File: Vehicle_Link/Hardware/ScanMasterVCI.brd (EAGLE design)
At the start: 53 x 39.4 mm, 96 parts, among them IC1 XMEGA32A4U, IC2 TL331, IC3 TL331, IC4 TL331, IC5 TL331, Q1 MMBT4403, Q10 ZXMP6A17G, Q2 MMBT3904, Q3 RUM002N05, Q5 RUM002N05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

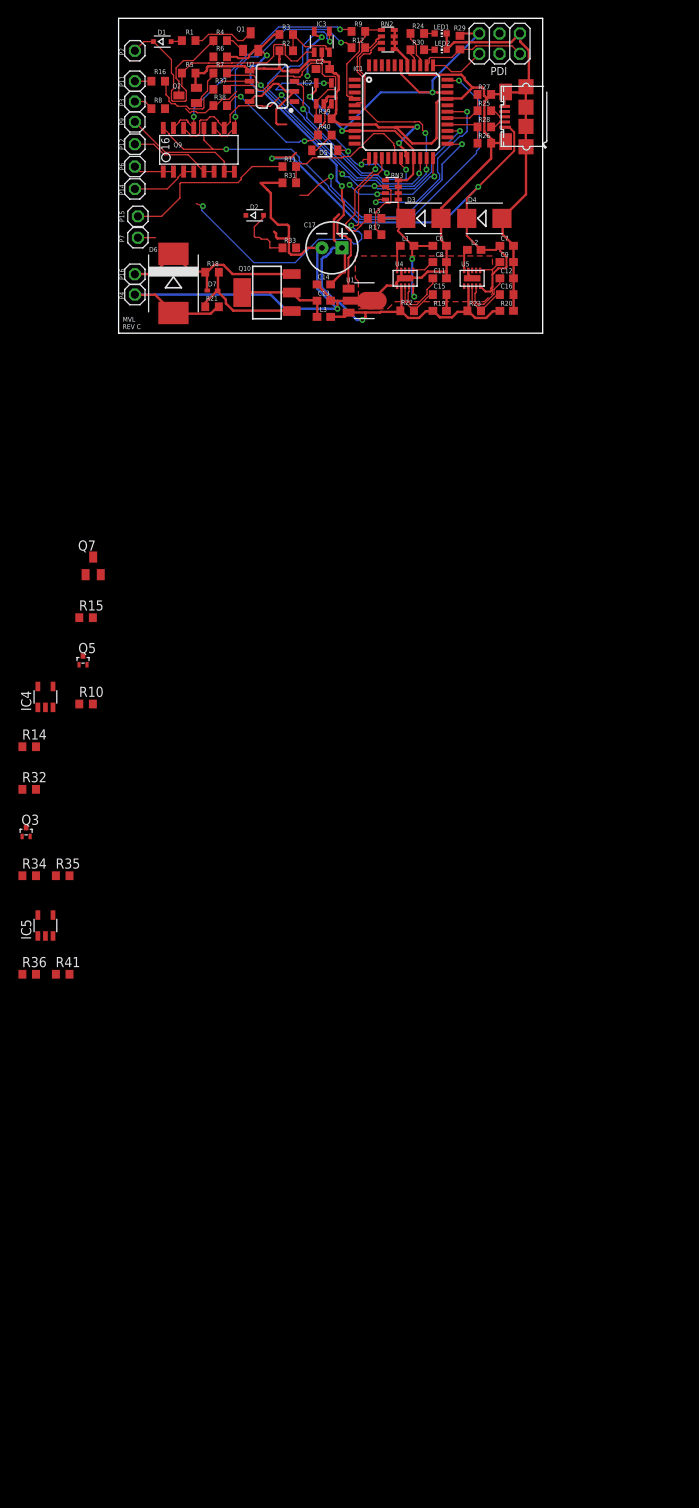
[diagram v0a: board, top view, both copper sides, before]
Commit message: Removed the BJTs I was using. Going to try the schematic with MOSFETs.
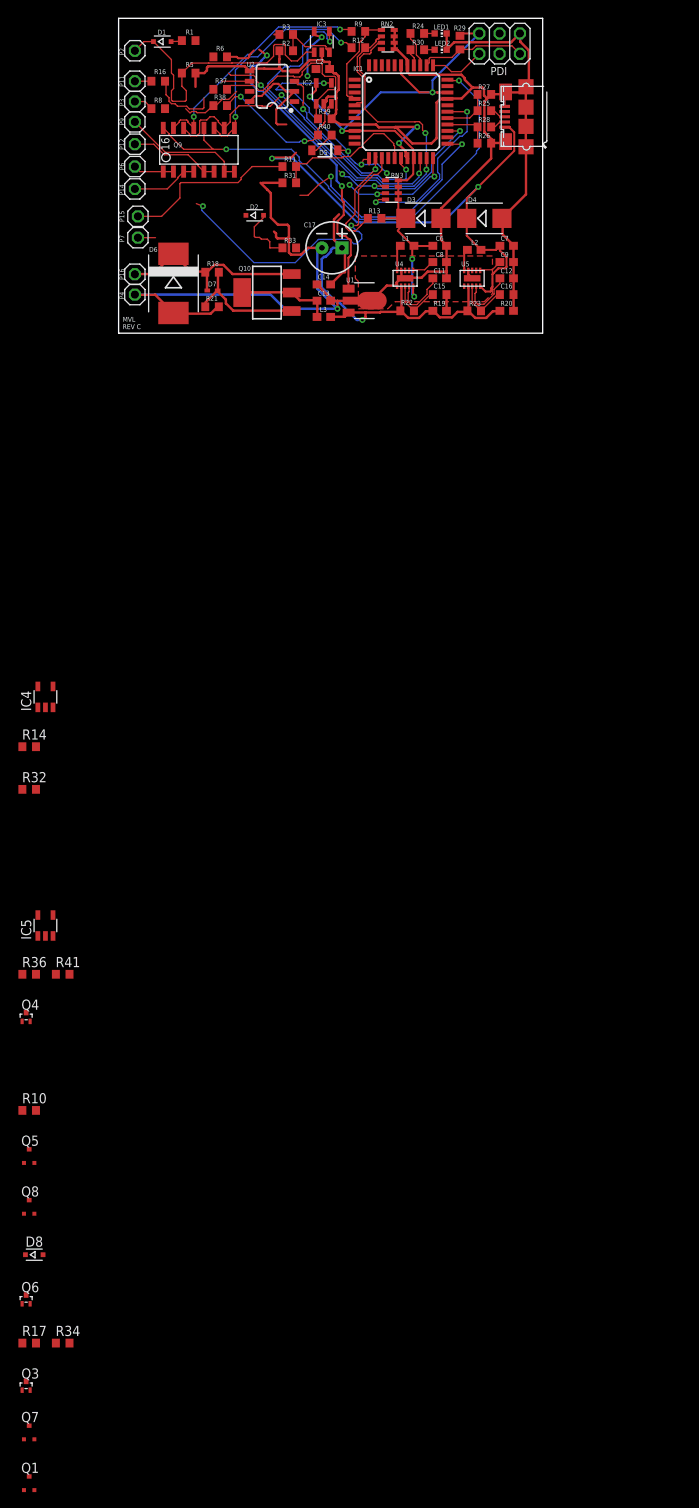
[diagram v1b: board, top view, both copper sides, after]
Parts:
- removed Q2: MMBT3904, semicon-smd-ipc:SOT23
- removed R15, R35, R7: 1k, adafruit:R0603
- removed R4: 5.1k, adafruit:R0603
- added D8: 1N4148WX, diode:SOD323-R
- added Q4, Q6: RUM002N05, customics:EMT3
- added Q8: RRF015P03, customics:SOT323
- Q1: value MMBT4403 -> RRF015P03; device transistor-pnp:SOT23-BEC -> customics:SOT323
- Q5: value RUM002N05 -> RRF015P03; device customics:EMT3 -> customics:SOT323
- Q7: value MMBT3904 -> RRF015P03; device semicon-smd-ipc:SOT23 -> customics:SOT323
- R10, R14, R2, R3, R32, R6: value 1k -> 10k
- R17, R34: value 470 -> 10k
- moved Q1 182.3 mm to (-11.2, -143.8)
- moved R17 145.1 mm to (-11.2, -126.2)
- moved Q7 108.6 mm to (-11.2, -137.4)
- moved Q3 69.2 mm to (-11.6, -131.6)
- moved Q5 62.3 mm to (-11.2, -102.9)
- moved R34 58.6 mm to (-6.99, -126.2)
- moved R10 51.3 mm to (-11.2, -97.2)
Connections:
- removed net ISO-K: D2.C, IC4.1, Q5.2, Q7.3
- removed net N$13: Q7.1, R15.1
- removed net N$28: Q1.B, R4.2
- removed net N$29: Q1.C, R1.1
- removed net N$6: Q2.1, R7.2
- removed net SCI-A-RX: IC5.1, Q3.2
- new net N$21: D8.A, R17.2
- new net N$22: Q5.3, R33.1
- new net N$23: Q6.3, Q8.1, R34.2
- new net N$31: Q8.3, R17.1
- net +12V: now also Q5.2, R10.1; no longer R33.1
- net +3V3: no longer R10.1, R35.1
- net +5V: now also Q8.2, R34.1
- net +8V: now also Q7.2; no longer Q1.E
- net GND: now also Q1.3, Q3.2, Q4.2, Q6.2; no longer Q2.2, Q7.2
- net ISO-K-EN: now also Q4.1, RN2.4; no longer R17.2, RN3.2
- net ISO-K-TX: now also Q3.1; no longer R15.2
- net J1850VPW-TX: now also Q1.1; no longer R7.1
- net J1962-7: now also D2.C, D8.C, IC4.1, IC5.1; no longer Q5.3
- net N$10: now also Q7.3, R1.1; no longer Q3.1, R34.1, R35.2
- net N$26: now also Q1.2, Q7.1; no longer Q2.3, R4.1
- net N$4: now also Q4.3; no longer R17.1
- net SCI-A-RX-EN: now also Q6.1; no longer R34.2
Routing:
- net N$26: track 10.3 -> 0.00 mm
- net ISO-K-EN: track 31.3 -> 22.8 mm
- net N$29: track 7.95 -> 0.00 mm
- net N$6: track 4.62 -> 0.00 mm
- net +8V: track 47.3 -> 43.2 mm
- net N$28: track 2.89 -> 0.00 mm

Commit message: Last set of commits for redesigning comm circuits (hopefully). I've tested all the circuits individually. Added the new connector for the OBD -> board connection.
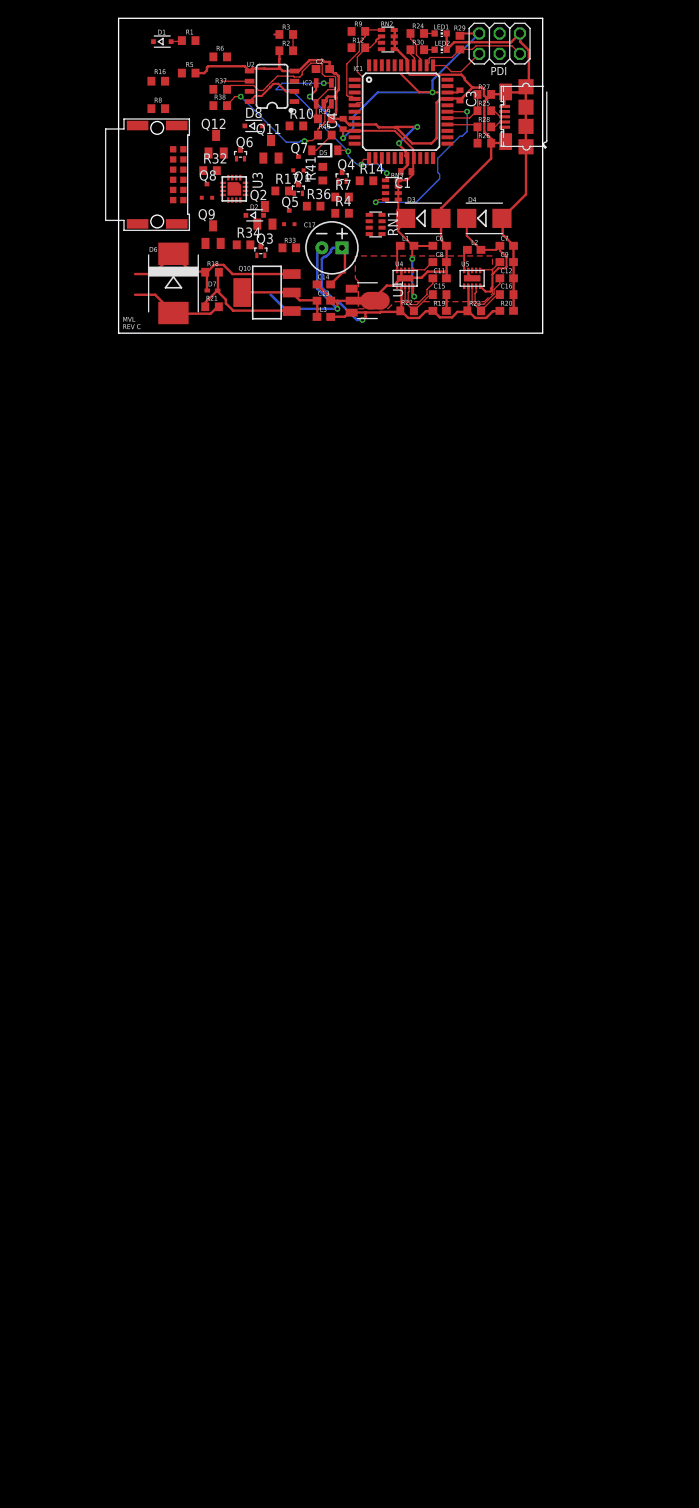
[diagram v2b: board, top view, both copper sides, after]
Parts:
- removed IC3, IC4, IC5: TL331, linear:DBV-R-PDSO-G5
- removed P11, P12, P14, P15, P16, P2, P3, P4, P6, P7, P9: (no value), pinhead:1X01
- removed R11, R13: 1k, adafruit:R0603
- removed R31: 2k, adafruit:R0603
- added C1, C3, C4: 100nF, adafruit:C0402
- added P1: HARFLEX-1515012-601, customics:HARFLEX-1515012-601
- added Q11, Q12, Q2: (no value), semicon-smd-ipc:SOT23
- added R4, R7: 1k, adafruit:R0603
- added RN1: 100k, resistor-net:CTS742C083
- added U3: LM339, customics:QFN16
- D6: value 1.5SMC43AT3G -> 1.5SMC43AT3G
- Q1: value RRF015P03 -> RUM002N05; device customics:SOT323 -> customics:EMT3
- Q9: value MMPQ3904 -> (none); device customics:SO-16 -> semicon-smd-ipc:SOT23
- U1: value L78L08ABUTR -> L78L
- U2: value MAX13444EASA+ -> MAX13444EASA+T
- moved Q1 165.3 mm to (22.5, 18.0)
- moved Q7 162.2 mm to (22.5, 21.2)
- moved R17 147.4 mm to (20.4, 17.8)
- moved Q6 145.6 mm to (15.2, 22.4)
- moved Q3 144.9 mm to (17.8, 10.3)
- moved D8 143.7 mm to (16.9, 25.9)
- moved R34 139.1 mm to (15.6, 11.0)
- moved Q8 128.9 mm to (11.0, 17.8)
- moved R10 127.5 mm to (22.2, 25.9)
- moved Q5 121.8 mm to (21.3, 14.5)
- moved Q4 112.2 mm to (27.9, 19.6)
- moved R41 105.2 mm to (25.5, 19.9), turned to 90 degrees
- moved R36 102.4 mm to (24.4, 15.9)
- moved R14 82.4 mm to (31.0, 19.1)
- moved R32 80.6 mm to (11.4, 20.3)
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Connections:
- new net N$6: R4.1, R7.2, U3.9
- net +12V: now also U3.1; no longer IC4.5, IC5.5
- net +3V3: now also C1.1, C3.1, C4.1; no longer IC3.5, R13.2
- net +5V: now also R4.2
- net CCD-TX: now also RN3.2; no longer R13.1
- net GND: now also C1.2, C3.2, C4.2, P1.6, Q1.2, R7.1, RN1.5, RN1.6, U3.12; no longer IC3.2, IC4.2, IC5.2, P4.1, Q1.3, R31.2
- net ISO-K-RX: now also U3.16; no longer IC4.4
- net ISO-K-TX: now also RN1.4
- net J1850VPW-RX: now also U3.14; no longer IC3.4
- net J1962-11: now also P1.10; no longer P11.1
- net J1962-12: now also P1.9, Q11.3; no longer P12.1, Q9.5, Q9.6
- net J1962-14: now also P1.4; no longer P14.1, Q9.4
- net J1962-15: now also P1.2, U3.11; no longer P15.1, R11.1
- net J1962-16: now also P1.7; no longer P16.1
- net J1962-2: now also P1.1, U3.8; no longer IC3.1, P2.1
- net J1962-3: now also P1.11; no longer P3.1
- net J1962-6: now also P1.5, Q2.3; no longer P6.1, Q9.1, Q9.2
- net J1962-7: now also P1.3, U3.4, U3.6; no longer IC4.1, IC5.1, P7.1
- net J1962-9: now also P1.8, Q12.3; no longer P9.1, Q9.7, Q9.8
- net N$1: now also Q2.1, Q9.1; no longer Q9.13, Q9.15
- net N$14: now also U3.5; no longer IC5.3
- net N$26: now also Q1.3; no longer Q1.2
- net N$37: now also U3.7; no longer IC3.3
- net N$5: now also Q11.1, Q12.1; no longer Q9.11, Q9.9
- net N$8: now also U3.2; no longer IC4.3
- net SCI-A-RX-EN: now also RN1.3
- net SCI-ENGINE-RX: now also U3.15; no longer IC5.4
- net SCI-ENGINE-TX: now also Q11.2, Q2.2; no longer Q9.12, Q9.16
- net SCI-TRANS-RX: now also U3.13; no longer R11.2, R31.1
- net SCI-TRANS-TX: now also Q12.2, Q9.2; no longer Q9.10, Q9.14
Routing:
- net SCI-ENGINE-TX: track 62.7 -> 0.00 mm, vias 2 -> 0
- net J1850VPW-TX: track 57.6 -> 0.00 mm, vias 3 -> 0
- net +5V: track 78.4 -> 23.1 mm, vias 2 -> 0
- net +8V: track 43.2 -> 0.66 mm, vias 2 -> 0
- net GND: track 264.9 -> 223.7 mm
- net J1850VPW-RX: track 41.1 -> 0.00 mm, vias 2 -> 0
- net SCI-TRANS-TX: track 40.5 -> 0.00 mm, vias 2 -> 0
- net SCI-A-RX-EN: track 38.9 -> 0.00 mm, vias 2 -> 0
- net J1962-2: track 37.7 -> 0.00 mm
- net ISO-K-TX: track 31.7 -> 0.00 mm, vias 2 -> 0
- net CCD-TX: track 31.8 -> 0.21 mm, vias 2 -> 0
- net N$1: track 30.1 -> 0.00 mm, vias 2 -> 0
- net N$5: track 28.5 -> 0.00 mm, vias 2 -> 0
- net ISO-K-EN: track 22.8 -> 0.00 mm, vias 3 -> 0
- net J1962-15: track 21.8 -> 0.00 mm
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
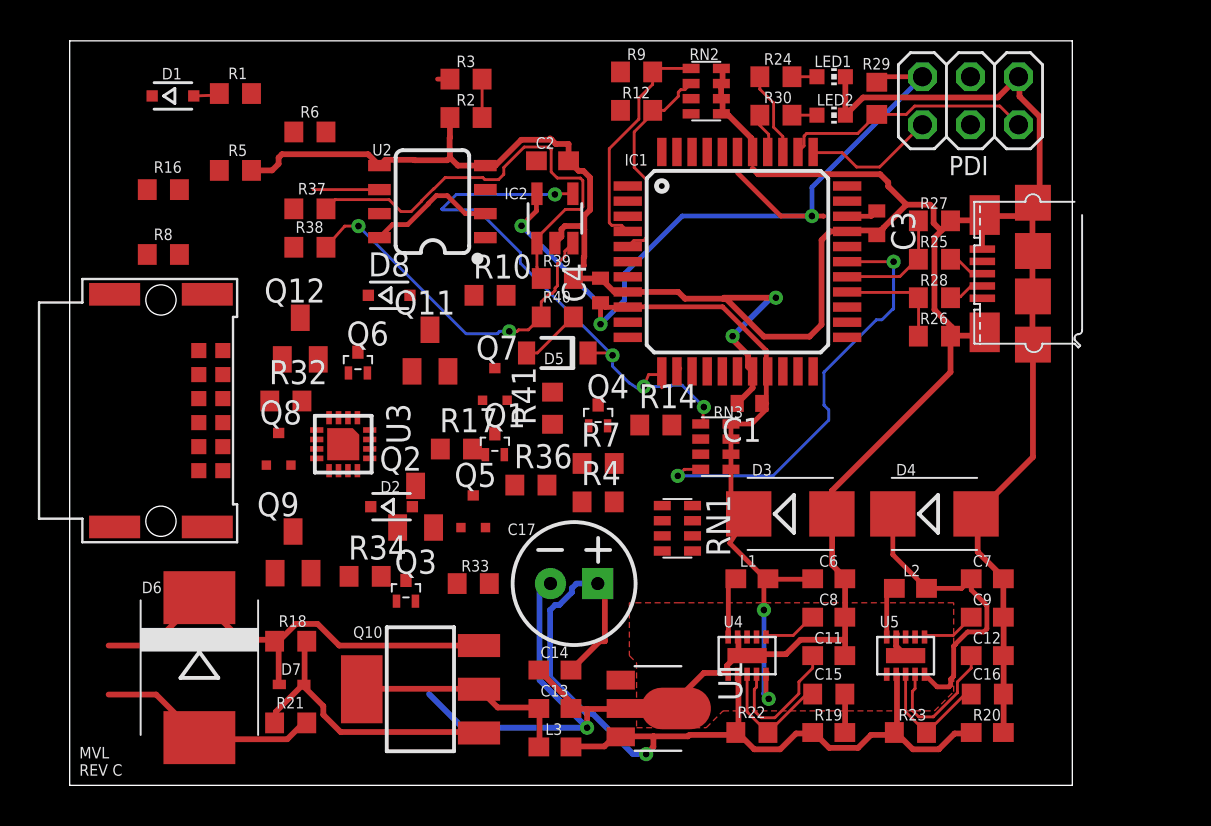
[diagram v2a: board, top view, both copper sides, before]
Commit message: Finally swapped out the USB connector for a Bluetooth module, BT823A. Finished the board layout with minimal changes to the comm circuits. Bumped the rev number to D
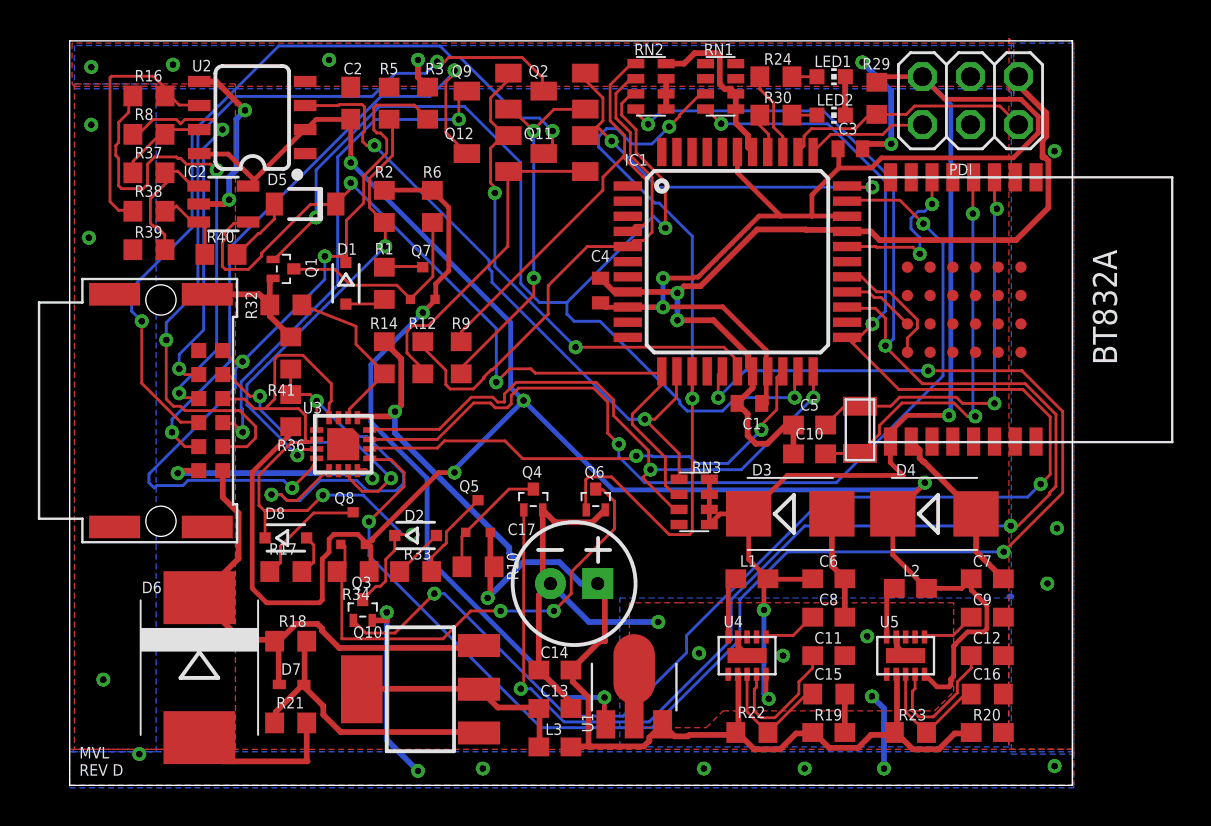
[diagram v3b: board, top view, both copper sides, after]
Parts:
- removed R25, R26: 33, adafruit:R0603
- removed R27, R28: 15k, adafruit:R0603
- removed R4, R7: 1k, adafruit:R0603
- removed U$1: MICRO_USB, customics:10118192
- added C10, C5: 12pF, SparkFun-Capacitors:0603
- added O1: 32.768khz, customics:FC-135
- added U6: BT832A, customics:BT832A
- moved Q9 26.5 mm to (22.1, 36.7), turned to 90 degrees
- moved RN1 23.5 mm to (34.4, 37.0)
- moved Q2 23.3 mm to (26.2, 36.7), turned to 90 degrees
- moved R39 21.6 mm to (4.19, 28.3), turned to 180 degrees
- moved R40 18.1 mm to (8.00, 28.1)
- moved R9 17.7 mm to (20.7, 22.6), turned to 270 degrees
- moved IC2 17.5 mm to (8.13, 30.7), turned to 270 degrees
- moved R12 17.3 mm to (18.7, 22.6), turned to 270 degrees
- moved D5 15.5 mm to (12.4, 30.7)
- moved R14 14.8 mm to (16.6, 22.6), turned to 90 degrees
- moved Q1 14.5 mm to (11.3, 27.3), turned to 270 degrees
- moved Q6 14.5 mm to (27.8, 15.1)
- moved R10 14.4 mm to (21.6, 11.6), turned to 180 degrees
- moved R41 14.1 mm to (11.7, 22.9), turned to 270 degrees
- moved D8 13.9 mm to (11.4, 13.1)
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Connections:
- removed net N$14: R36.1, R41.2, U3.5
- removed net N$25: R26.1, U$1.2
- removed net SCI-A-TX-EN: IC1.28, RN3.4
- removed net USB_D+: IC1.27, R25.2, R27.1
- removed net USB_D-: IC1.26, R26.2, R28.1
- new net BT-MODE: IC1.29, U6.6
- new net BT-RX: IC1.26, U6.C5
- new net BT-TX: IC1.27, U6.D5
- new net N$13: C5.2, O1.2, U6.3
- net +3V3: now also U6.9
- net +5V: no longer R4.2, U$1.1
- net CCD-RX: now also RN3.2; no longer RN3.1
- net CCD-TX: now also RN3.1; no longer RN3.2
- net GND: now also C10.1, C5.1, P1.7, P1.NC1, P1.NC2, P1.NC3, P1.NC4, U6.10, U6.A0, U6.B0, U6.C0, U6.D0; no longer P1.6, R27.2, R28.2, R7.1, U$1.5, U$1.M1, U$1.M2, U$1.M3, U$1.M4, U$1.M5, U$1.M6
- net J1962-16: now also P1.6; no longer P1.7
- net N$24: now also C10.2, O1.1, U6.4; no longer R25.1, U$1.3
- net N$6: now also R36.1, R41.2, U3.5; no longer R4.1, R7.2
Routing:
- net ISO-K-EN: track 0.00 -> 88.4 mm, vias 0 -> 4
- net ISO-K-TX: track 0.00 -> 82.4 mm, vias 0 -> 4
- net +5V: track 23.1 -> 103.4 mm, vias 0 -> 4
- net SCI-TRANS-RX: track 0.00 -> 79.6 mm, vias 0 -> 4
- net J1850VPW-TX: track 0.00 -> 60.9 mm, vias 0 -> 3
- net GND: track 223.7 -> 166.9 mm, vias 3 -> 31
- net SCI-ENGINE-RX: track 0.00 -> 50.7 mm, vias 0 -> 2
- net J1962-6: track 0.00 -> 43.6 mm, vias 0 -> 2
- net J1962-12: track 0.00 -> 42.9 mm, vias 0 -> 2
- net J1962-2: track 0.00 -> 41.0 mm, vias 0 -> 3
- net SCI-A-RX-EN: track 0.00 -> 40.5 mm, vias 0 -> 2
- net +8V: track 0.66 -> 39.1 mm, vias 0 -> 2
- net J1962-7: track 0.00 -> 36.1 mm, vias 0 -> 2
- net ISO-K-RX: track 0.07 -> 34.1 mm, vias 0 -> 2
- net CCD-TX: track 0.21 -> 34.1 mm, vias 0 -> 2
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- added copper zone on layer 16, net GND
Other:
- board text added: "MVL REV D"
- board text removed: "MVL REV C"
